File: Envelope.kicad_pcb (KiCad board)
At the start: 2 copper layers, 39.6 x 100 mm, 0 parts

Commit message: Lots of further work.
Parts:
- added C1: 100n, Capacitors_SMD:C_0805, F.Cu at (148.8, 146.3)
- added C2: 100n, Capacitors_SMD:C_0805, F.Cu at (146.4, 150.9)
- added C3: 100n, Capacitors_SMD:C_0805, F.Cu at (148.2, 161.6)
- added C4: 100n, Capacitors_SMD:C_0805, F.Cu at (162.9, 157.6)
- added C5: 22p, Capacitors_SMD:C_0805, F.Cu at (142.2, 154.5)
- added C6: 22p, Capacitors_SMD:C_0805, F.Cu at (142.2, 158.1)
- added J1: Conn_02x03_Odd_Even, Pin_Headers:Pin_Header_Straight_2x03_Pitch2.54mm, F.Cu at (166.5, 168.7)
- added J2: Conn_01x06, Pin_Headers:Pin_Header_Straight_1x06_Pitch2.54mm, F.Cu at (136.9, 145.3)
- added R1: 10k, Resistors_SMD:R_0805, F.Cu at (162.4, 153.0)
- added SW1: RST, Buttons_Switches_THT:SW_PUSH_6mm_h13mm, F.Cu at (171.0, 164.3)
- added U1: ATMEGA328P-AU, Housings_QFP:TQFP-32_7x7mm_Pitch0.8mm, B.Cu at (126.6, 105.8)
- added U2: L7805, TO_SOT_Packages_SMD:TO-263-2, F.Cu at (130.4, 182.4)
- added Y1: Crystal, Crystals:Crystal_SMD_5032-2pin_5.0x3.2mm, F.Cu at (146.1, 156.3)

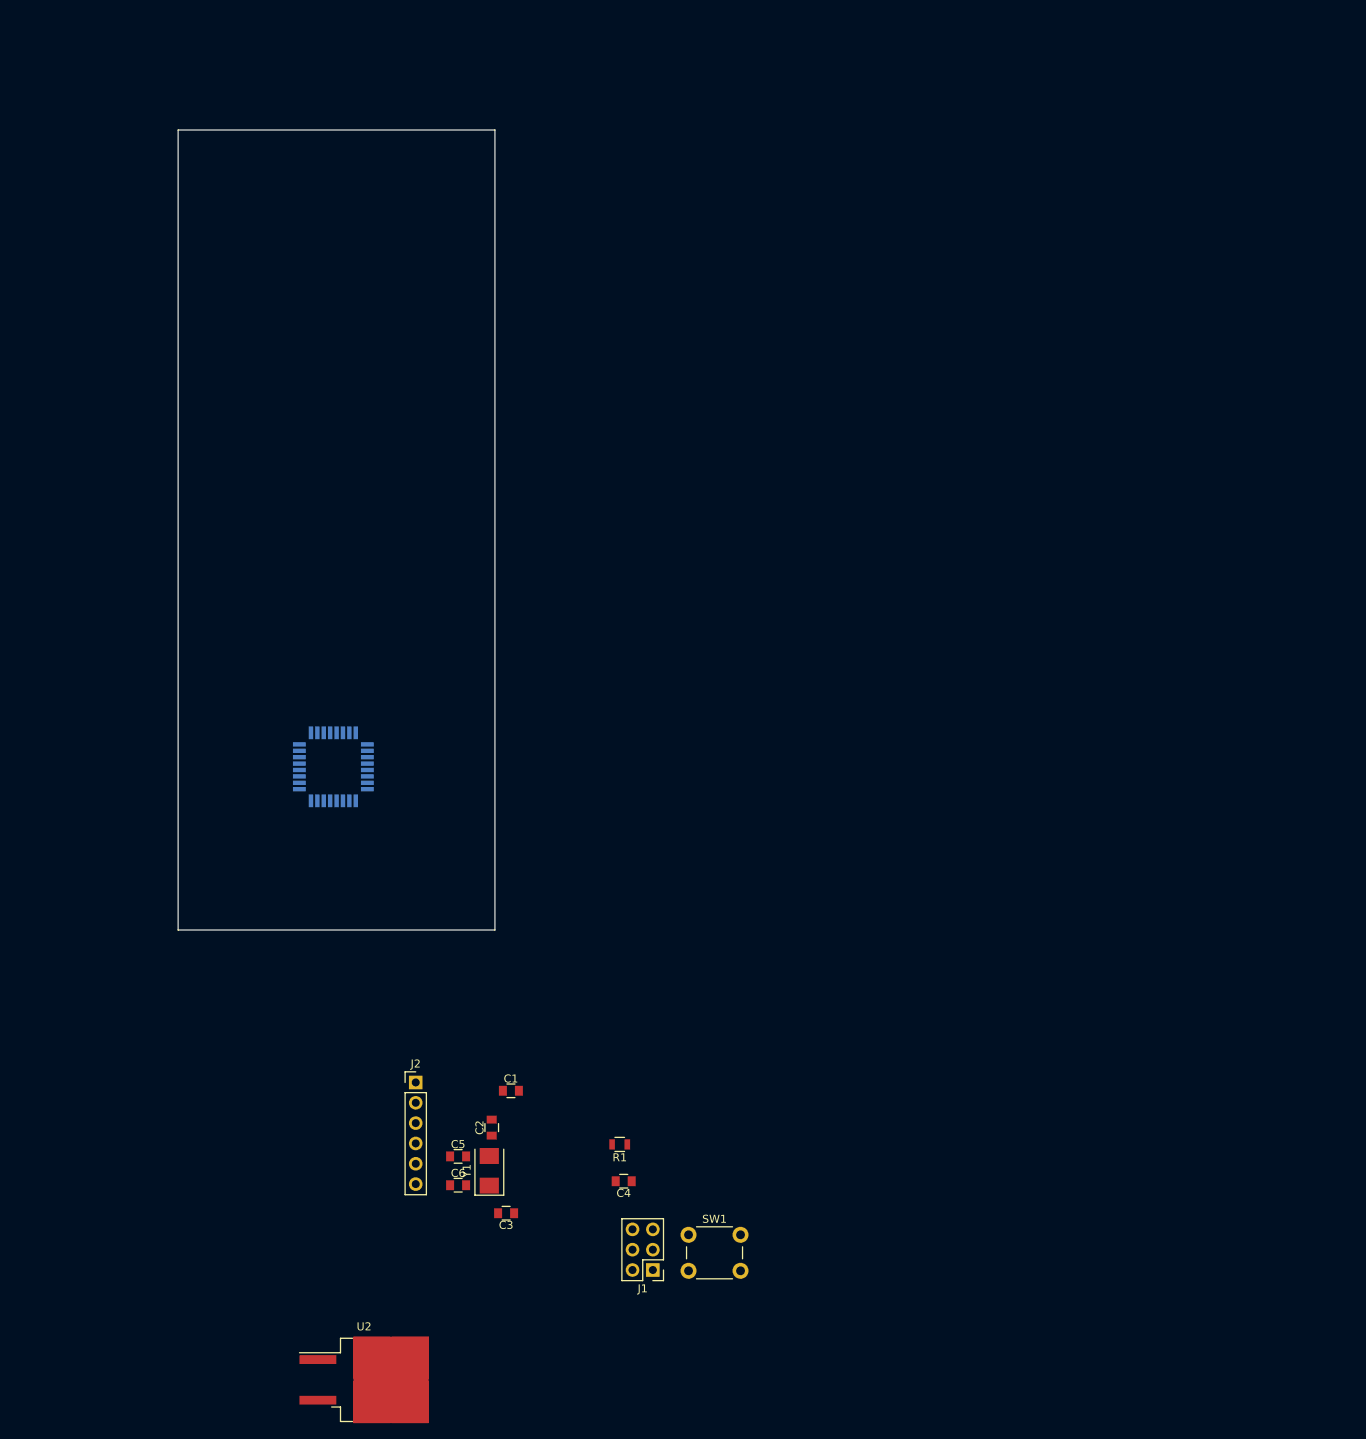
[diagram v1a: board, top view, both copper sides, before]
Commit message: Use new jacks.
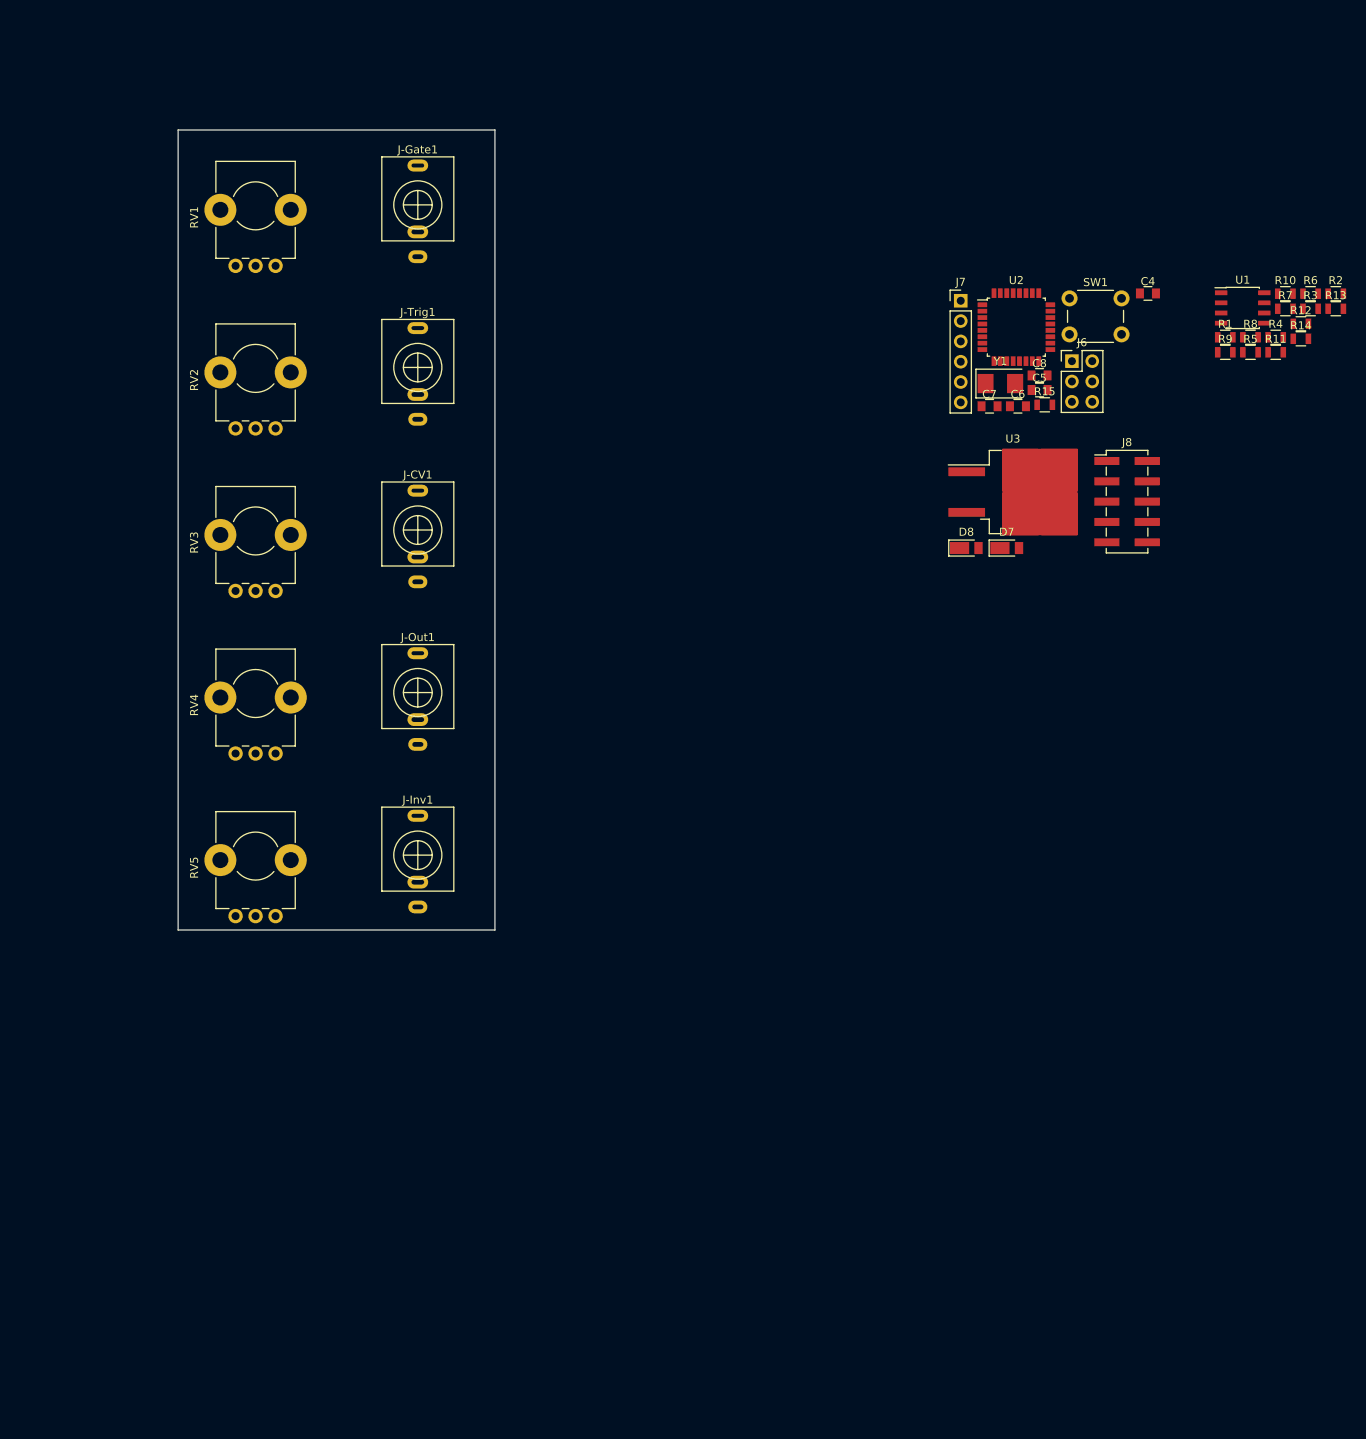
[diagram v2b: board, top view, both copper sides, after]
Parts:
- removed C1, C2, C3: 100n, Capacitors_SMD:C_0805
- removed J1: Conn_02x03_Odd_Even, Pin_Headers:Pin_Header_Straight_2x03_Pitch2.54mm
- removed J2: Conn_01x06, Pin_Headers:Pin_Header_Straight_1x06_Pitch2.54mm
- added C7: 22p, Capacitors_SMD:C_0805, F.Cu at (208.6, 60.7)
- added C8: 22p, Capacitors_SMD:C_0805, F.Cu at (214.9, 56.9)
- added D7: DFLR1400-7, Diodes_SMD:D_PowerDI-123, F.Cu at (210.8, 78.5)
- added D8: DFLR1400-7, Diodes_SMD:D_PowerDI-123, F.Cu at (205.7, 78.5)
- added J-CV1: AudioJack2_Ground_Switch, Local:PJ398SM, F.Cu at (137.2, 76.2)
- added J-Gate1: AudioJack2_Ground_Switch, Local:PJ398SM, F.Cu at (137.2, 35.6)
- added J-Inv1: AudioJack2_Ground_Switch, Local:PJ398SM, F.Cu at (137.2, 116.8)
- added J-Out1: AudioJack2_Ground_Switch, Local:PJ398SM, F.Cu at (137.2, 96.5)
- added J-Trig1: AudioJack2_Ground_Switch, Local:PJ398SM, F.Cu at (137.2, 55.9)
- added J6: Conn_02x03_Odd_Even, Pin_Headers:Pin_Header_Straight_2x03_Pitch2.54mm, F.Cu at (218.9, 55.1)
- added J7: Conn_01x06, Pin_Headers:Pin_Header_Straight_1x06_Pitch2.54mm, F.Cu at (205.0, 47.5)
- added J8: Conn_02x05_Odd_Even, Pin_Headers:Pin_Header_Straight_2x05_Pitch2.54mm_SMD, F.Cu at (225.8, 72.7)
- added R10: 100k, Resistors_SMD:R_0805, F.Cu at (245.6, 46.7)
- added R11: 1k, Resistors_SMD:R_0805, F.Cu at (244.4, 54.0)
- added R12: 100k, Resistors_SMD:R_0805, F.Cu at (247.5, 50.4)
- added R13: 47k, Resistors_SMD:R_0805, F.Cu at (251.9, 48.5)
- added R14: 4k7, Resistors_SMD:R_0805, F.Cu at (247.5, 52.3)
- added R15: 10k, Resistors_SMD:R_0805, F.Cu at (215.5, 60.6)
- added R2: 4k7, Resistors_SMD:R_0805, F.Cu at (251.9, 46.7)
- added R3: 47k, Resistors_SMD:R_0805, F.Cu at (248.8, 48.5)
- added R4: 4k7, Resistors_SMD:R_0805, F.Cu at (244.4, 52.1)
- added R5: R, Resistors_SMD:R_0805, F.Cu at (241.2, 54.0)
- added R6: R, Resistors_SMD:R_0805, F.Cu at (248.8, 46.7)
- added R7: R, Resistors_SMD:R_0805, F.Cu at (245.6, 48.5)
- added R8: 1k, Resistors_SMD:R_0805, F.Cu at (241.2, 52.1)
- added R9: 100k, Resistors_SMD:R_0805, F.Cu at (238.1, 54.0)
- added RV1: POT, Potentiometers:Potentiometer_Alps_RK09K_Horizontal, F.Cu at (119.4, 43.2)
- added RV2: POT, Potentiometers:Potentiometer_Alps_RK09K_Horizontal, F.Cu at (119.4, 63.5)
- added RV3: POT, Potentiometers:Potentiometer_Alps_RK09K_Horizontal, F.Cu at (119.4, 83.8)
- added RV4: POT, Potentiometers:Potentiometer_Alps_RK09K_Horizontal, F.Cu at (119.4, 104.1)
- added RV5: POT, Potentiometers:Potentiometer_Alps_RK09K_Horizontal, F.Cu at (119.4, 124.5)
- added U3: L7805, TO_SOT_Packages_SMD:TO-263-2, F.Cu at (211.5, 71.5)
- C5, C6: value 22p -> 100n
- R1: value 10k -> 47k
- U1: value ATMEGA328P-AU -> TL072; footprint Housings_QFP:TQFP-32_7x7mm_Pitch0.8mm -> Housings_SOIC:SOIC-8_3.9x4.9mm_Pitch1.27mm; moved to F.Cu
- U2: value L7805 -> ATmega328PB-AU; footprint TO_SOT_Packages_SMD:TO-263-2 -> Housings_QFP:LQFP-32_7x7mm_Pitch0.8mm
- moved U2 154.8 mm to (212.0, 50.8)
- moved C4 128.9 mm to (228.4, 46.6), turned to 0 degrees
- moved U1 127.3 mm to (240.3, 48.4), turned to 0 degrees
- moved SW1 126.4 mm to (218.6, 47.2)
- moved R1 126.1 mm to (238.1, 52.1), turned to 0 degrees
- moved C5 120.2 mm to (214.9, 58.7)
- moved C6 119.9 mm to (212.2, 60.7)
- moved Y1 117.3 mm to (210.0, 57.9), turned to 0 degrees
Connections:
- net Net-(U2-Pad3) renamed /MCU328/PE0
- C4 pad 1: VCC -> +5V
- C5 pad 2: Net-(C5-Pad2) -> +5V
- C6 pad 1: GND -> Net-(C6-Pad1)
- C6 pad 2: Net-(C6-Pad2) -> GND
- R1 pad 1: VCC -> Net-(D1-Pad2)
- R1 pad 2: Net-(J1-Pad5) -> Net-(J-Gate1-PadT)
- SW1 pad 1: Net-(J1-Pad5) -> Net-(J6-Pad1)
- U1 pad 1: /MCU328/PD3 -> Net-(R10-Pad1)
- U1 pad 2: /MCU328/PD4 -> Net-(R10-Pad1)
- U1 pad 3: GND -> Net-(C3-Pad1)
- U1 pad 4: VCC -> -12V
- U1 pad 5: GND -> (no net)
- U1 pad 6: VCC -> (no net)
- U1 pad 7: Net-(C5-Pad2) -> (no net)
- U1 pad 8: Net-(C6-Pad2) -> +12V
- U2 pad 1: Net-(U2-Pad1) -> /MCU328/PD3
- U2 pad 2: Net-(U2-Pad2) -> /MCU328/PD4
- Y1 pad 1: Net-(C6-Pad2) -> Net-(C8-Pad2)
- Y1 pad 2: Net-(C5-Pad2) -> Net-(C7-Pad2)

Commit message: Assigned more footprints.
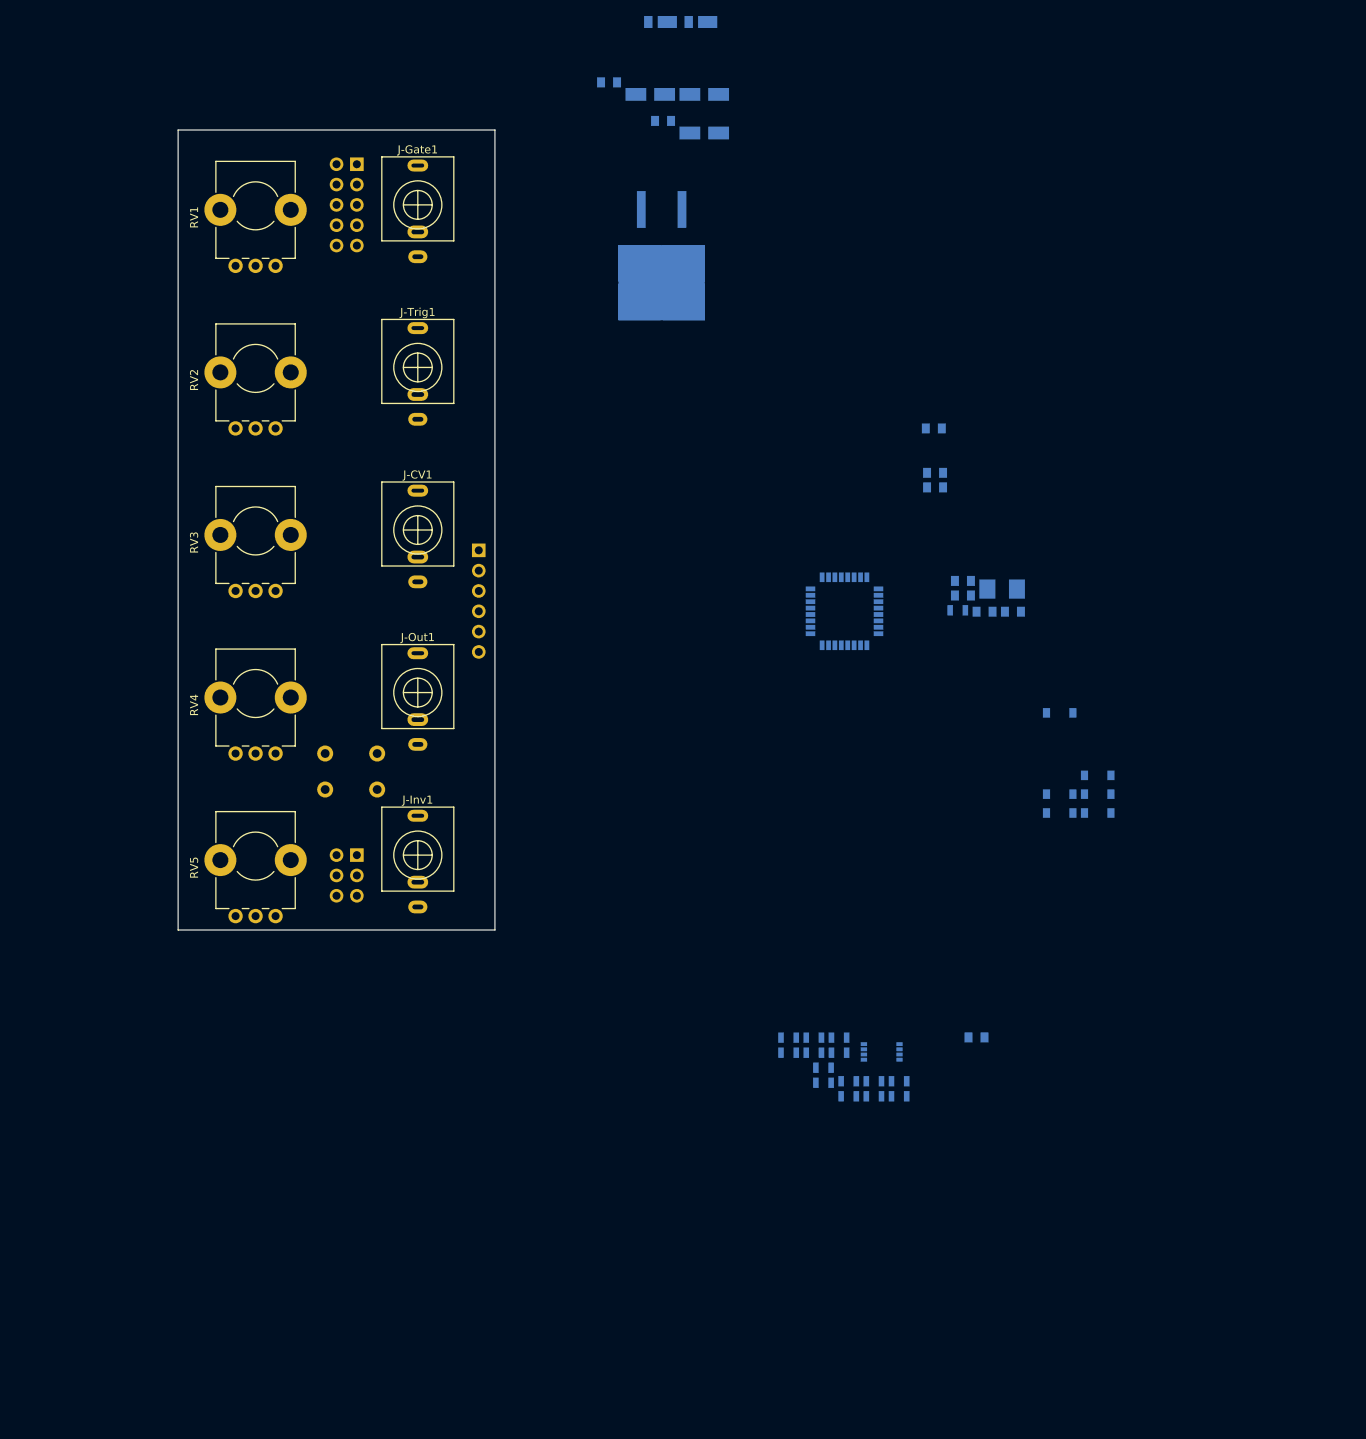
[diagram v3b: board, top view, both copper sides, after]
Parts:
- added C1: C, Capacitors_SMD:C_0805, B.Cu at (201.7, 63.5)
- added C10: 100n, Capacitors_SMD:C_0805, B.Cu at (161.1, 20.2)
- added C11: 100n, Capacitors_SMD:C_0805, B.Cu at (167.8, 25.1)
- added C12: 10u, Capacitors_SMD:CP_Elec_4x5.8, B.Cu at (173.0, 26.6)
- added C13: 10u, Capacitors_SMD:CP_Elec_4x5.8, B.Cu at (173.0, 21.7)
- added C2: C, Capacitors_SMD:C_0805, B.Cu at (201.8, 69.1)
- added C3: C, Capacitors_SMD:C_0805, B.Cu at (201.8, 70.9)
- added C9: 10u, Capacitors_SMD:CP_Elec_4x5.8, B.Cu at (166.2, 21.7)
- added D1: 1N5819, Diodes_SMD:D_SOD-123, B.Cu at (217.4, 111.6)
- added D2: 1N5819, Diodes_SMD:D_SOD-123, B.Cu at (222.1, 109.2)
- added D3: 1N5819, Diodes_SMD:D_SOD-123, B.Cu at (222.1, 106.9)
- added D4: 1N5819, Diodes_SMD:D_SOD-123, B.Cu at (217.4, 99.1)
- added D5: 1N5819, Diodes_SMD:D_SOD-123, B.Cu at (222.1, 111.6)
- added D6: 1N5819, Diodes_SMD:D_SOD-123, B.Cu at (217.4, 109.2)
- C4, C5, C6, C7, C8, D7, D8, J6, J7, R1, R10, R11, R12, R13, R14, R15, R2, R3, R4, R5, R6, R7, R8, R9, SW1, U2, U3, Y1: moved to B.Cu
- J8: footprint Pin_Headers:Pin_Header_Straight_2x05_Pitch2.54mm_SMD -> Pin_Headers:Pin_Header_Straight_2x05_Pitch2.54mm; moved to B.Cu
- U1: footprint Housings_SOIC:SOIC-8_3.9x4.9mm_Pitch1.27mm -> Housings_SSOP:OnSemi_Micro8; moved to B.Cu
- moved R13 115.4 mm to (183.5, 141.5), turned to 180 degrees
- moved R2 115.4 mm to (183.5, 139.7), turned to 180 degrees
- moved R3 111.8 mm to (186.7, 141.5), turned to 180 degrees
- moved R6 111.8 mm to (186.7, 139.7), turned to 180 degrees
- moved R12 110.5 mm to (187.9, 143.4), turned to 180 degrees
- moved R14 110.5 mm to (187.9, 145.3), turned to 180 degrees
- moved J6 108.6 mm to (129.5, 116.8), turned to 180 degrees
- moved R10 108.4 mm to (189.8, 139.7), turned to 180 degrees
- moved R7 108.4 mm to (189.8, 141.5), turned to 180 degrees
- moved R11 107.2 mm to (191.0, 147.0), turned to 180 degrees
- moved R4 107.2 mm to (191.0, 145.1), turned to 180 degrees
- moved J8 105.1 mm to (129.5, 30.5), turned to 180 degrees
- moved R8 104.2 mm to (194.2, 145.1), turned to 180 degrees
- moved R5 104.2 mm to (194.2, 147.0), turned to 180 degrees
- moved SW1 103.6 mm to (132.1, 104.1), turned to 180 degrees
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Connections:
- U1 pad 5: (no net) -> Net-(U1-Pad5)
- U1 pad 6: (no net) -> Net-(U1-Pad6)
- U1 pad 7: (no net) -> Net-(R11-Pad2)
